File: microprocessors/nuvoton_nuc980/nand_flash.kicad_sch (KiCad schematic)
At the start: 7 parts, among them U8 MX30LF1G28AD-XKI

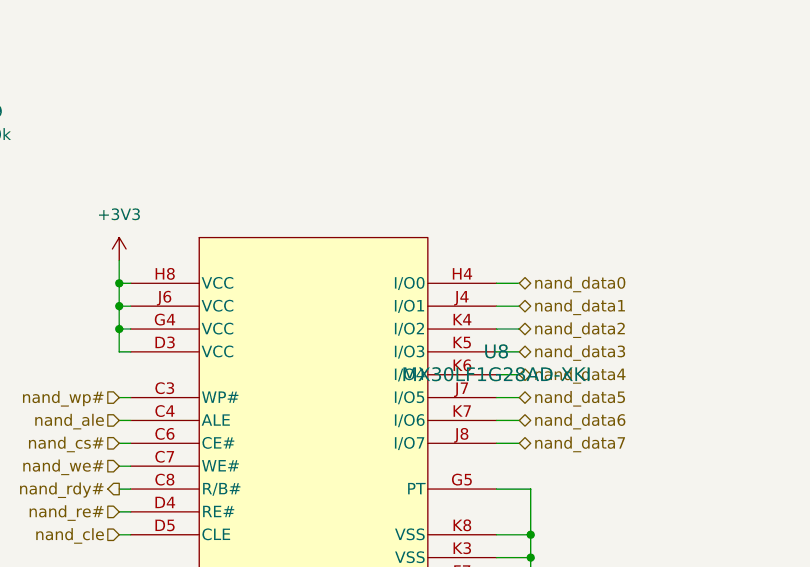
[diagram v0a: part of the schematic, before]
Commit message: feat: ERC passing cotti-nuvoton
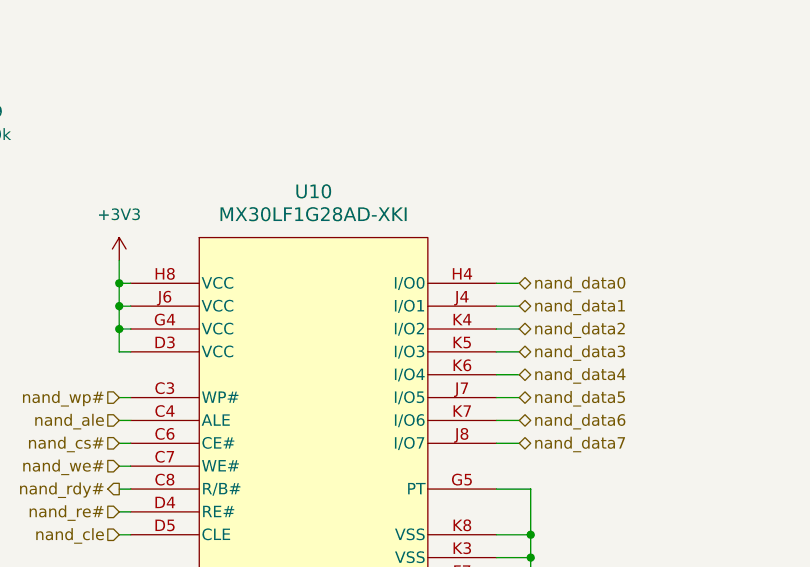
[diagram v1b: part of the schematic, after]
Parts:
- removed U8: MX30LF1G28AD-XKI, VFBGA63_9X11_MAC, symbol cotti_mem:MX30LF1G28AD-XKI
- added U10: MX30LF1G28AD-XKI, cotti_footprints:VFBGA63_9X11_MAC-M, symbol cotti_mem:MX30LF1G28AD-XKI
- C43, C44, C45, C46: footprint (none) -> Capacitor_SMD:C_0805_2012Metric_Pad1.18x1.45mm_HandSolder; Digikey (none) -> https://www.digikey.com/en/products/detail/samsung-electro-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; Mfr. (none) -> Samsung Electro-Mechanics; Mfr. P/N (none) -> CL21B104KACNNNC
- R10, R9: footprint (none) -> Resistor_SMD:R_0805_2012Metric_Pad1.20x1.40mm_HandSolder; Digikey (none) -> https://www.digikey.com/en/products/detail/yageo/RC0805FR-1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; Mfr. (none) -> YAGEO; Mfr. P/N (none) -> RC0805FR-1310KL
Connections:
- net +3V3: now also U10.D3 (VCC), U10.G4 (VCC), U10.H8 (VCC), U10.J6 (VCC)
- net GND: now also U10.C5 (VSS), U10.F7 (VSS), U10.G5 (PT), U10.K3 (VSS), U10.K8 (VSS)
- net nand_ale: now also U10.C4 (ALE)
- net nand_cle: now also U10.D5 (CLE)
- net nand_cs#: now also U10.C6 (CE#)
- net nand_data0: now also U10.H4 (I/O0)
- net nand_data1: now also U10.J4 (I/O1)
- net nand_data2: now also U10.K4 (I/O2)
- net nand_data3: now also U10.K5 (I/O3)
- net nand_data4: now also U10.K6 (I/O4)
- net nand_data5: now also U10.J7 (I/O5)
- net nand_data6: now also U10.K7 (I/O6)
- net nand_data7: now also U10.J8 (I/O7)
- net nand_rdy#: now also U10.C8 (R/B#)
- net nand_re#: now also U10.D4 (RE#)
- net nand_we#: now also U10.C7 (WE#)
- net nand_wp#: now also U10.C3 (WP#)
